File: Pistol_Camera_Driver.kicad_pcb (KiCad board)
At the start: 2 copper layers, 95.8 x 46.1 mm, 70 parts, among them J1 Screw_Terminal_01x02, J10 Screw_Terminal_01x02, J11 Screw_Terminal_01x02, J12 I2C, J13 Screw_Terminal_01x02, J14 Bluetooth, J15 I2C, J16 I2C, J2 Screw_Terminal_01x02, J3 Objective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

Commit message: v0.2 DRC passed
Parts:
- moved C3 16.1 mm to (76.2, 41.6), turned to 90 degrees
- moved C4 9.36 mm to (100.8, 72.5)
- moved J3 9.24 mm to (106.5, 56.9)
- moved C10 9.22 mm to (103.0, 41.5)
- moved C11 9.22 mm to (100.2, 43.4)
- moved C12 9.22 mm to (103.6, 43.5)
- moved C7 9.22 mm to (101.5, 70.5)
- moved C8 9.22 mm to (98.2, 70.5)
- moved R10 9.22 mm to (93.8, 63.5)
- moved R11 9.22 mm to (98.0, 59.6)
- moved R13 9.22 mm to (102.6, 60.0)
- moved R14 9.22 mm to (94.3, 66.5)
- moved R15 9.22 mm to (105.7, 50.8)
- moved R18 9.22 mm to (98.9, 54.6)
- moved R3 9.22 mm to (95.5, 63.5)
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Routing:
- net +3V3: track 139.0 -> 122.8 mm
- net MOTORS_nSLEEP: track 88.9 -> 75.6 mm
- net nFLT1: track 63.6 -> 53.1 mm, vias 4 -> 3
- net +3.3VP: track 112.5 -> 103.4 mm
- net nEN1: track 73.8 -> 65.0 mm
- net nFLT2: track 83.3 -> 75.0 mm
- net STEP1: track 60.6 -> 52.3 mm
- net DIR1: track 58.1 -> 51.0 mm
- net STEP2: track 47.7 -> 41.1 mm
- net nEN2: track 51.2 -> 44.6 mm
- net DIR2: track 43.5 -> 37.3 mm
- net Net-(C8-Pad1): track 23.9 -> 29.7 mm
- net +12V: track 75.3 -> 72.1 mm
- net GND: track 10.2 -> 12.8 mm, vias 305 -> 282
- net Net-(D2-Pad1): track 10.3 -> 12.0 mm
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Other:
- board size 95.8 x 46.1 mm -> 88.3 x 46.1 mm
- board text added: "Для ООО Теофота, в. 1.0, 2024г"

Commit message: v0.3 Seems 2B ready
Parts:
- R1, R2, R21, R22, R4, R5, R6, R7: moved to B.Cu
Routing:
- net Net-(R1-Pad1): track 13.3 -> 11.5 mm, vias 2 -> 0
- net nFLT2: track 75.0 -> 76.0 mm
- net GND: track 12.8 -> 12.6 mm, vias 282 -> 301
- net +5V: track 179.8 -> 180.0 mm, vias 1 -> 3
- net +3V3: track 122.8 -> 123.0 mm, vias 6 -> 5
- net Net-(J10-Pad1): vias 0 -> 1
- net +3.3VP: vias 0 -> 13

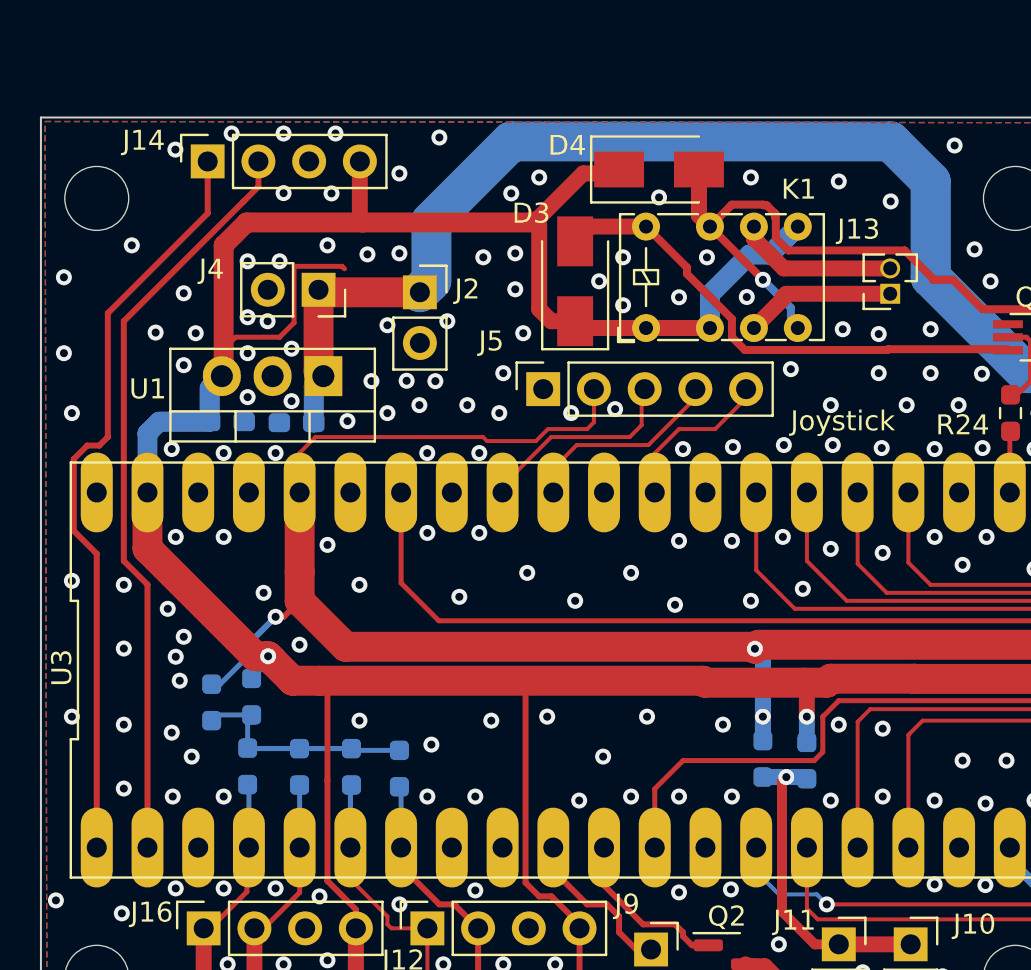
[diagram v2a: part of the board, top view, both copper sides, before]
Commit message: v0.4 5th I2C connector was added. Seems 2B ready.
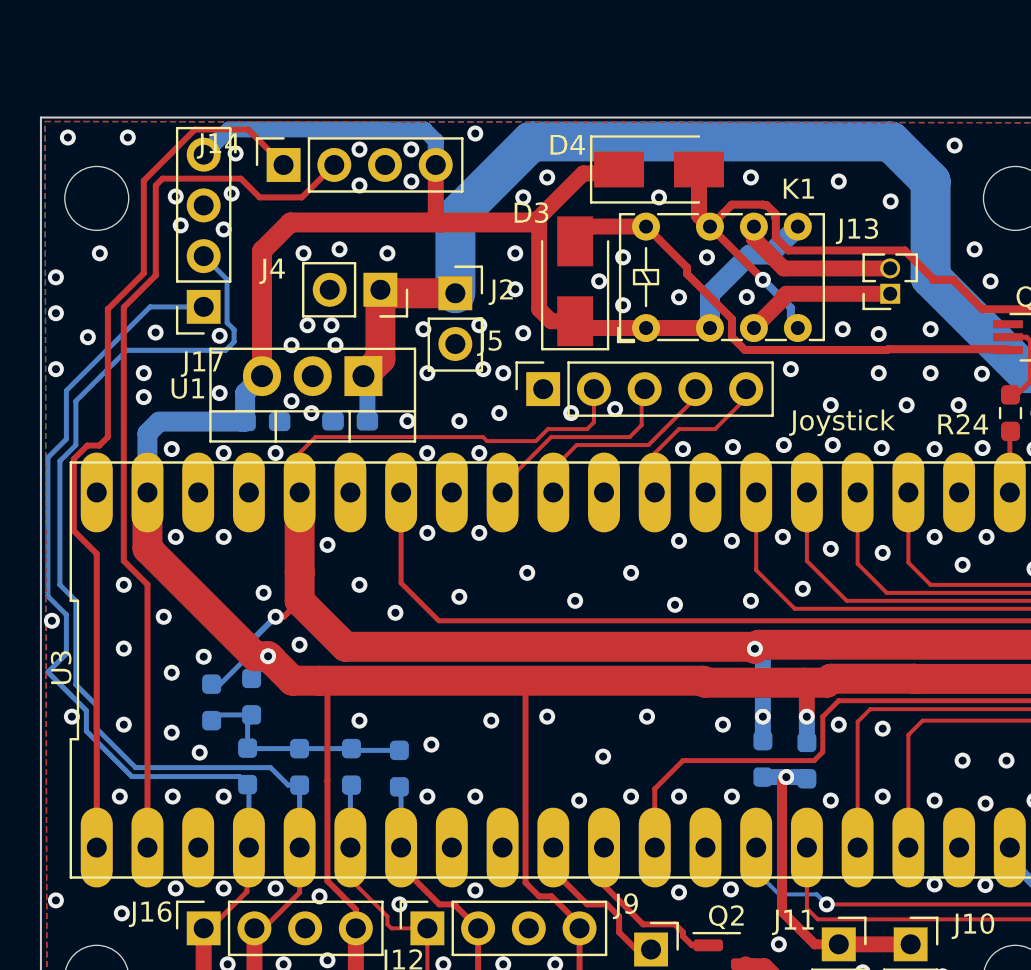
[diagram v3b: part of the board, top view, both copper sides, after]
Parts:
- added J17: I2C, Connector_PinSocket_2.54mm:PinSocket_1x04_P2.54mm_Vertical, F.Cu at (33.0, 41.1)
- moved J14 3.80 mm to (37.0, 34.0)
- moved J4 3.10 mm to (41.9, 40.2)
- moved C1 2.69 mm to (40.3, 46.8)
- moved U1 2.01 mm to (41.0, 44.5)
- moved J2 1.78 mm to (45.6, 40.4)
- moved C2 1.77 mm to (35.9, 46.8)
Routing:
- net SCL1: track 12.4 -> 55.3 mm
- net SDA1: track 12.0 -> 48.8 mm
- net TX: track 37.6 -> 44.5 mm
- net RX: track 38.0 -> 44.5 mm
- net +12V: track 72.1 -> 69.4 mm
- net +5V: track 180.0 -> 182.3 mm

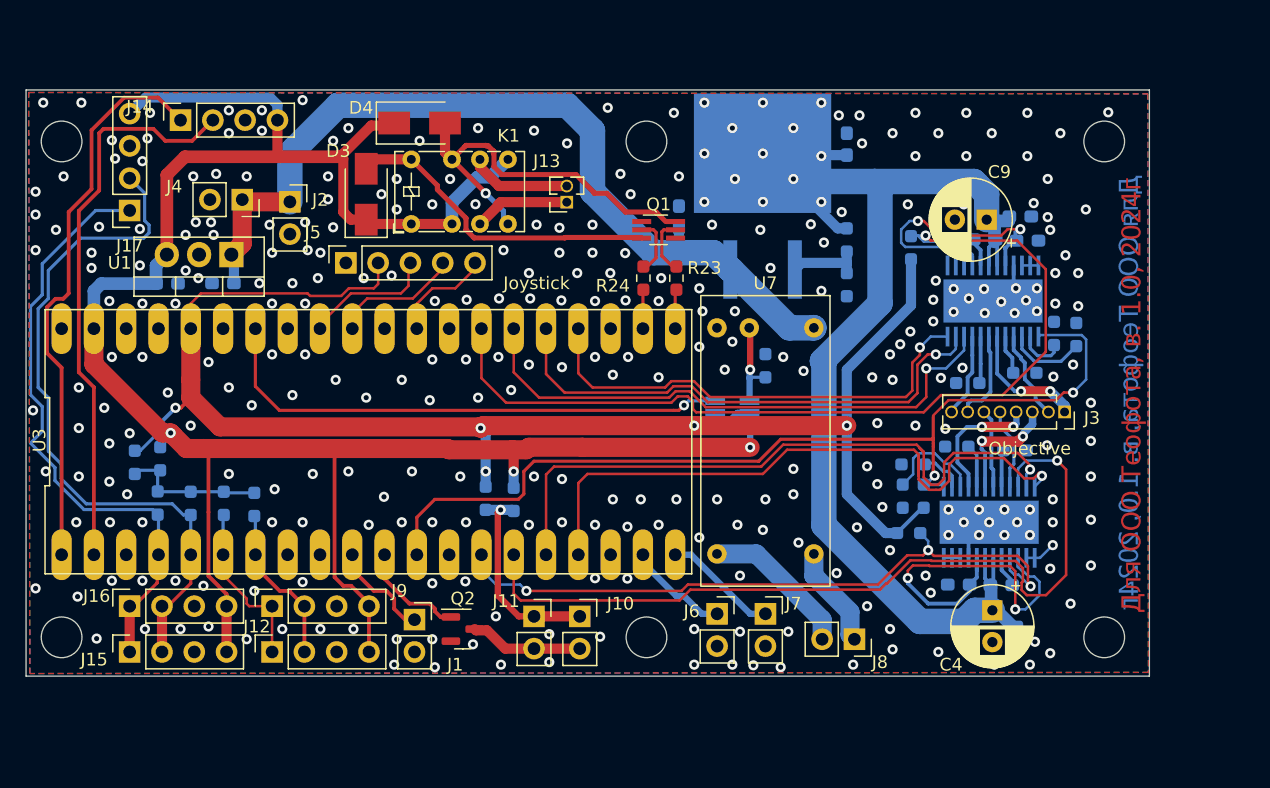
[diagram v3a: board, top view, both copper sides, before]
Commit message: v0.5 I2C multiplexer, 5 I2C cnnectors, dirty routing
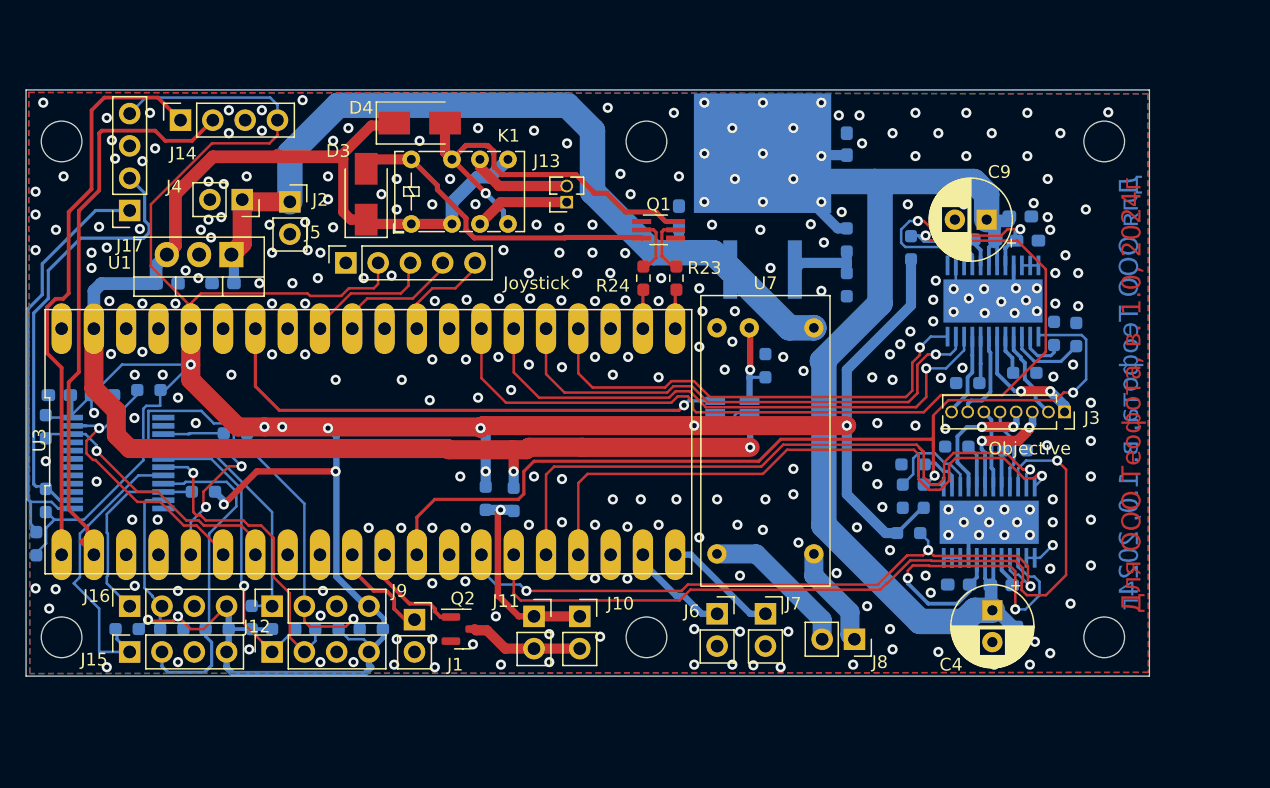
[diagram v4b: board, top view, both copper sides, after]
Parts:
- removed R2: 0, Resistor_SMD:R_0603_1608Metric_Pad0.98x0.95mm_HandSolder
- added C13: 0.1, Capacitor_SMD:C_0603_1608Metric_Pad1.08x0.95mm_HandSolder, B.Cu at (27.5, 55.6)
- added C14: 0.01, Capacitor_SMD:C_0603_1608Metric_Pad1.08x0.95mm_HandSolder, B.Cu at (30.9, 55.6)
- added R25: 4.7k, Resistor_SMD:R_0603_1608Metric_Pad0.98x0.95mm_HandSolder, B.Cu at (48.5, 74.0)
- added R26: 4.7k, Resistor_SMD:R_0603_1608Metric_Pad0.98x0.95mm_HandSolder, B.Cu at (45.1, 74.0)
- added R27: 4.7k, Resistor_SMD:R_0603_1608Metric_Pad0.98x0.95mm_HandSolder, B.Cu at (26.4, 63.9)
- added R28: 4.7k, Resistor_SMD:R_0603_1608Metric_Pad0.98x0.95mm_HandSolder, B.Cu at (25.7, 67.3)
- added R29: 4.7k, Resistor_SMD:R_0603_1608Metric_Pad0.98x0.95mm_HandSolder, B.Cu at (36.3, 74.0)
- added R30: 4.7k, Resistor_SMD:R_0603_1608Metric_Pad0.98x0.95mm_HandSolder, B.Cu at (38.8, 63.2)
- added R31: 4.7k, Resistor_SMD:R_0603_1608Metric_Pad0.98x0.95mm_HandSolder, B.Cu at (39.9, 74.0)
- added R32: 4.7k, Resistor_SMD:R_0603_1608Metric_Pad0.98x0.95mm_HandSolder, B.Cu at (32.8, 74.0)
- added U8: PCA9548ADB, Package_SO:SSOP-24_5.3x8.2mm_P0.65mm, B.Cu at (32.0, 60.9)
- R1: value 0 -> 4.7k
- moved R4 19.5 mm to (52.0, 74.0), turned to 180 degrees
- moved R7 17.5 mm to (26.4, 58.1)
- moved R6 10.7 mm to (34.5, 55.2), turned to 180 degrees
- moved R5 10.2 mm to (42.6, 73.1), turned to 90 degrees
- moved R1 6.24 mm to (41.3, 58.6), turned to 180 degrees
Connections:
- J12 pad 1: SDA0 -> Net-(J12-Pin_1)
- J12 pad 2: SCL0 -> Net-(J12-Pin_2)
- J12 pad 4: +5V -> +3V3
- J14 pad 4: +5V -> +3V3
- J15 pad 1: SDA1 -> Net-(J15-Pin_1)
- J15 pad 2: SCL1 -> Net-(J15-Pin_2)
- J15 pad 4: +5V -> +3V3
- J16 pad 1: SDA1 -> Net-(J16-Pin_1)
- J16 pad 2: SCL1 -> Net-(J16-Pin_2)
- J16 pad 4: +5V -> +3V3
- J17 pad 1: SDA1 -> Net-(J17-Pin_1)
- J17 pad 2: SCL1 -> Net-(J17-Pin_2)
- J17 pad 4: +5V -> +3V3
- J9 pad 1: SDA0 -> Net-(J9-Pin_1)
- J9 pad 2: SCL0 -> Net-(J9-Pin_2)
- J9 pad 4: +5V -> +3V3
- R1 pad 1: Net-(R1-Pad1) -> +3V3
- R1 pad 2: +5V -> I2C_RES
- R4 pad 1: Net-(R1-Pad1) -> +3V3
- R4 pad 2: SDA1 -> Net-(J9-Pin_2)
- R5 pad 1: Net-(R1-Pad1) -> +3V3
- R5 pad 2: SCL1 -> Net-(J9-Pin_1)
- R6 pad 1: Net-(R1-Pad1) -> +3V3
- R7 pad 1: Net-(R1-Pad1) -> +3V3
- U3 pad 4: SDA1 -> unconnected-(U3-GP2-Pad4)
- U3 pad 5: SCL1 -> I2C_RES
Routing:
- net +3V3: track 123.0 -> 262.6 mm, vias 5 -> 13
- net SCL1: track 55.3 -> 0.00 mm
- net +5V: track 182.3 -> 130.8 mm, vias 3 -> 2
- net SDA1: track 48.8 -> 0.00 mm
- net Net-(J9-Pin_2): track 0.00 -> 34.9 mm, vias 0 -> 1
- net Net-(J17-Pin_2): track 0.00 -> 34.9 mm
- net Net-(J17-Pin_1): track 0.00 -> 33.7 mm
- net Net-(J15-Pin_2): track 0.00 -> 26.5 mm
- net Net-(J12-Pin_2): track 0.00 -> 24.9 mm, vias 0 -> 1
- net Net-(J12-Pin_1): track 0.00 -> 23.5 mm, vias 0 -> 1
- net Net-(J15-Pin_1): track 0.00 -> 23.4 mm
- net Net-(J9-Pin_1): track 0.00 -> 19.8 mm
- net I2C_RES: track 0.00 -> 17.7 mm, vias 0 -> 2
- net Net-(J16-Pin_1): track 0.00 -> 15.9 mm
- net SDA0: track 13.5 -> 26.7 mm, vias 0 -> 1
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
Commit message: v0.6 thermal sensors, led strips, i2c Multiplexer were added. Ordered!
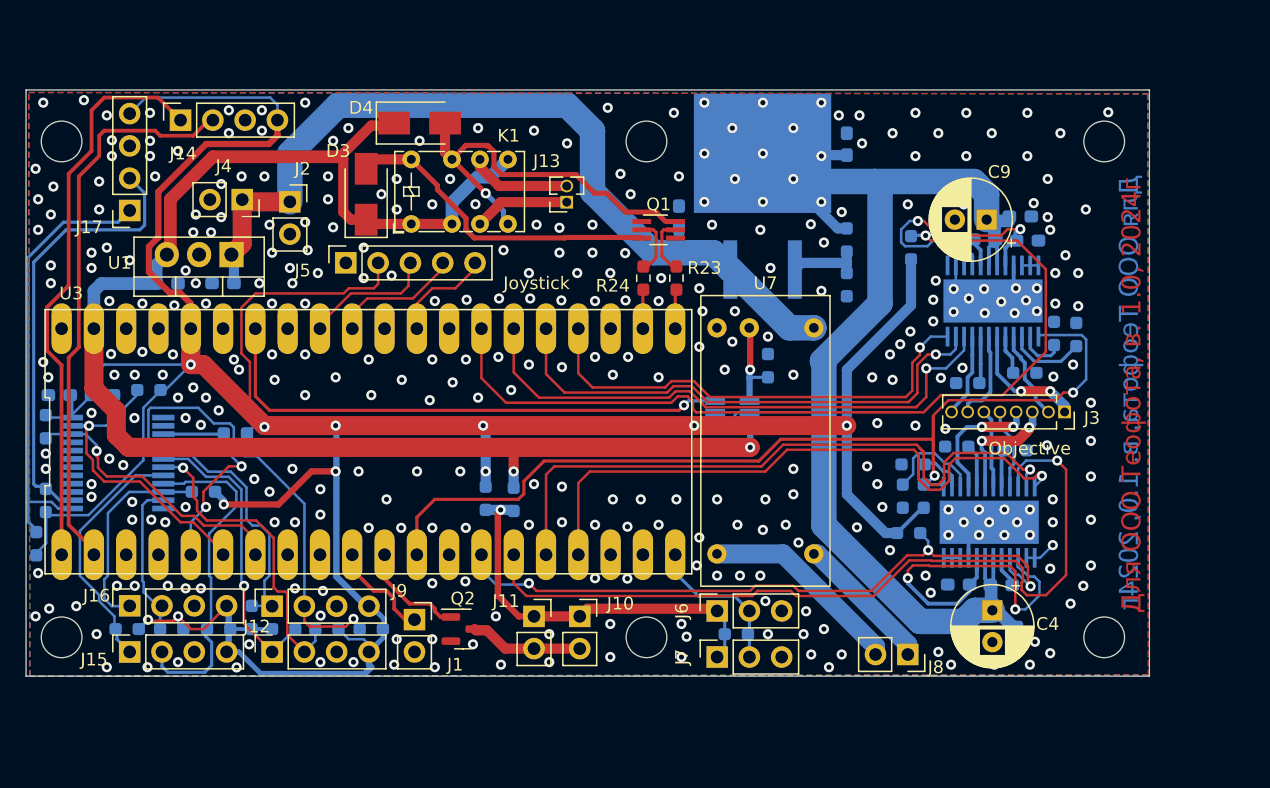
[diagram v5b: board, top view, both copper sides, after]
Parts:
- added R2: 4k7, Resistor_SMD:R_0603_1608Metric_Pad0.98x0.95mm_HandSolder, B.Cu at (80.7, 74.4)
- J6, J7: value Screw_Terminal_01x02 -> Conn_01x03_Socket; footprint Connector_PinSocket_2.54mm:PinSocket_1x02_P2.54mm_Vertical -> Connector_PinSocket_2.54mm:PinSocket_1x03_P2.54mm_Vertical
- moved J7 5.10 mm to (79.2, 76.2), turned to 90 degrees
- moved J8 4.37 mm to (94.2, 76.0)
- moved J6 0.22 mm to (79.2, 72.6), turned to 90 degrees
- moved R20 0.20 mm to (83.2, 53.3)
- moved R31 0.12 mm to (40.0, 74.0)
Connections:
- J10 pad 1: Net-(J10-Pin_1) -> V_lasers
- J11 pad 1: Net-(J10-Pin_1) -> V_lasers
- J6 pad 1: K1 -> V_lasers
- J6 pad 2: GND -> Thermo
- J7 pad 1: K2 -> V_lasers
- J7 pad 2: GND -> Thermo
- R21 pad 1: Net-(J10-Pin_1) -> V_lasers
- R22 pad 1: Net-(J10-Pin_1) -> V_lasers
- U3 pad 19: K1 -> unconnected-(U3-GP14-Pad19)
- U3 pad 20: K2 -> Thermo
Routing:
- net V_lasers: track 0.00 -> 31.4 mm, vias 0 -> 1
- net Net-(J10-Pin_1): track 16.2 -> 0.00 mm, vias 1 -> 0
- net Thermo: track 0.00 -> 13.1 mm
- net K2: track 9.02 -> 0.00 mm
- net K1: track 8.12 -> 0.00 mm
- net Net-(J8-Pin_2): track 12.0 -> 16.1 mm
- net Net-(J15-Pin_1): track 23.4 -> 19.5 mm
- net +5V: track 130.8 -> 127.3 mm
- net +3V3: track 262.6 -> 265.7 mm, vias 13 -> 11
- net Net-(J8-Pin_1): track 8.30 -> 11.1 mm
- net Net-(J17-Pin_1): track 33.7 -> 34.9 mm
- net TX: track 45.5 -> 44.6 mm
- net Net-(J16-Pin_1): track 15.9 -> 16.8 mm
- net SCL0: track 23.7 -> 24.4 mm
- net Net-(J9-Pin_1): track 19.8 -> 20.5 mm
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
